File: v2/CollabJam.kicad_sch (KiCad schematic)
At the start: 35 parts, among them IC1 SIP32510DT-T1-GE3, IC2 DA7281-00V4C, IC3 DA7281-00V4C, IC4 DA7281-00V4C, IC5 DA7281-00V4C, J1 Power, J10 ESP32 right, J11 ESP32 left, J2 ESP_BAT_GND, J3 ESP_BAT_PWR, M1 M1, M2 M2, M3 M3, M4 M4

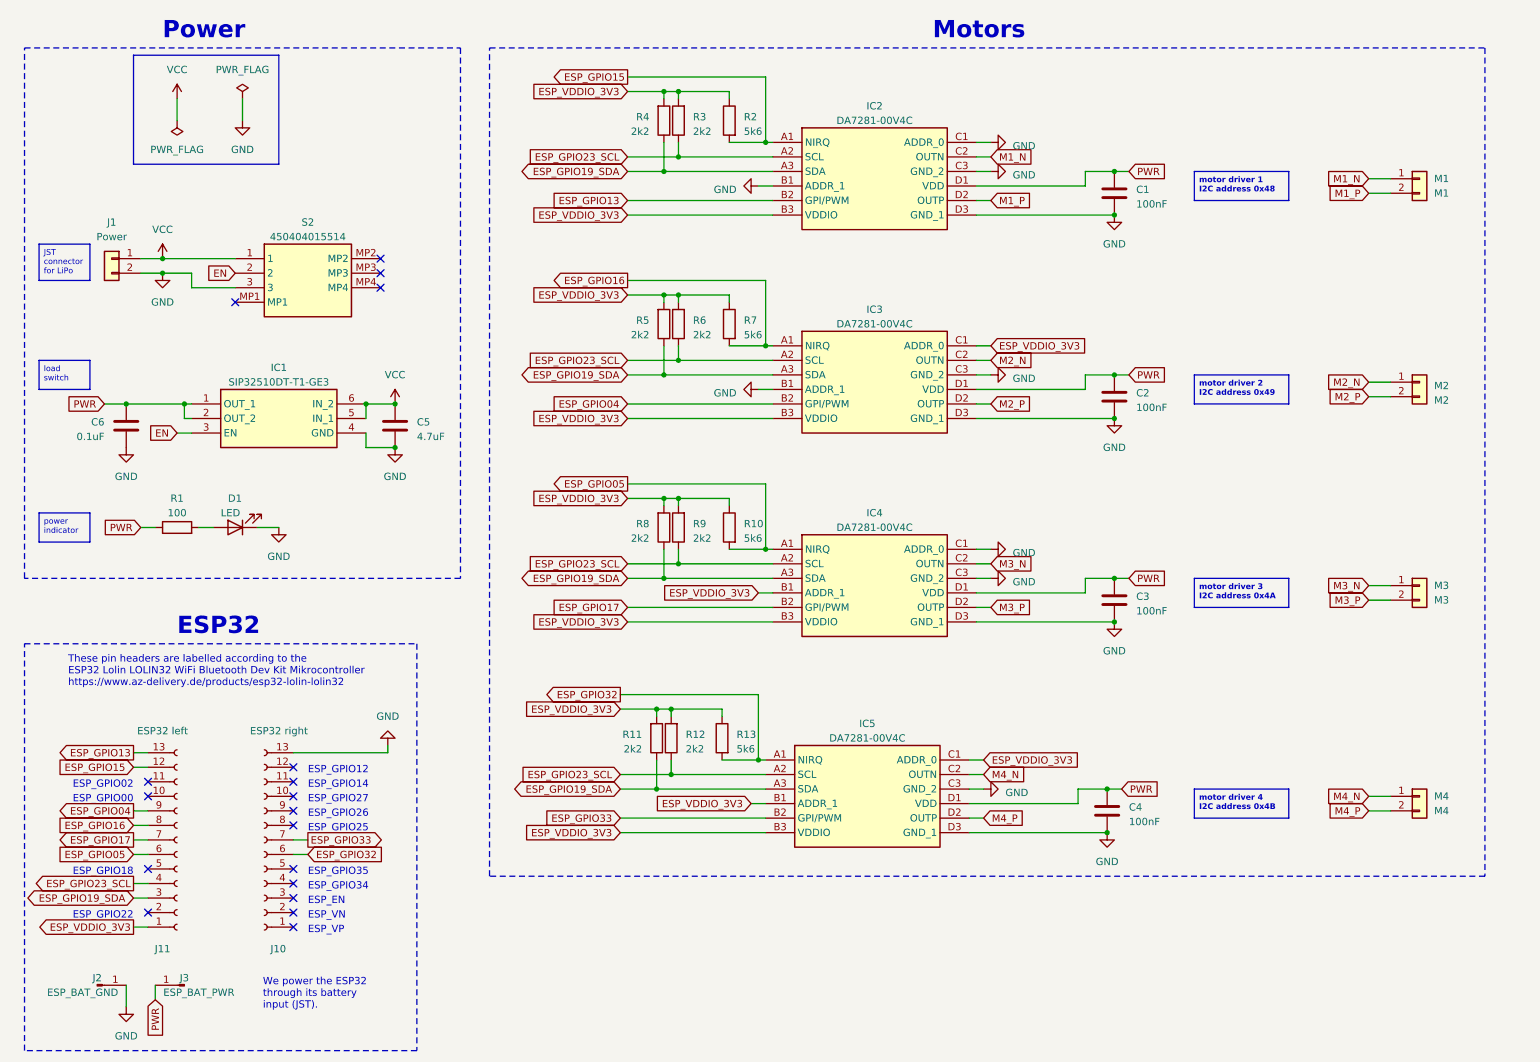
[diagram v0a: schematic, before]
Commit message: switch to QFN package for DA7281
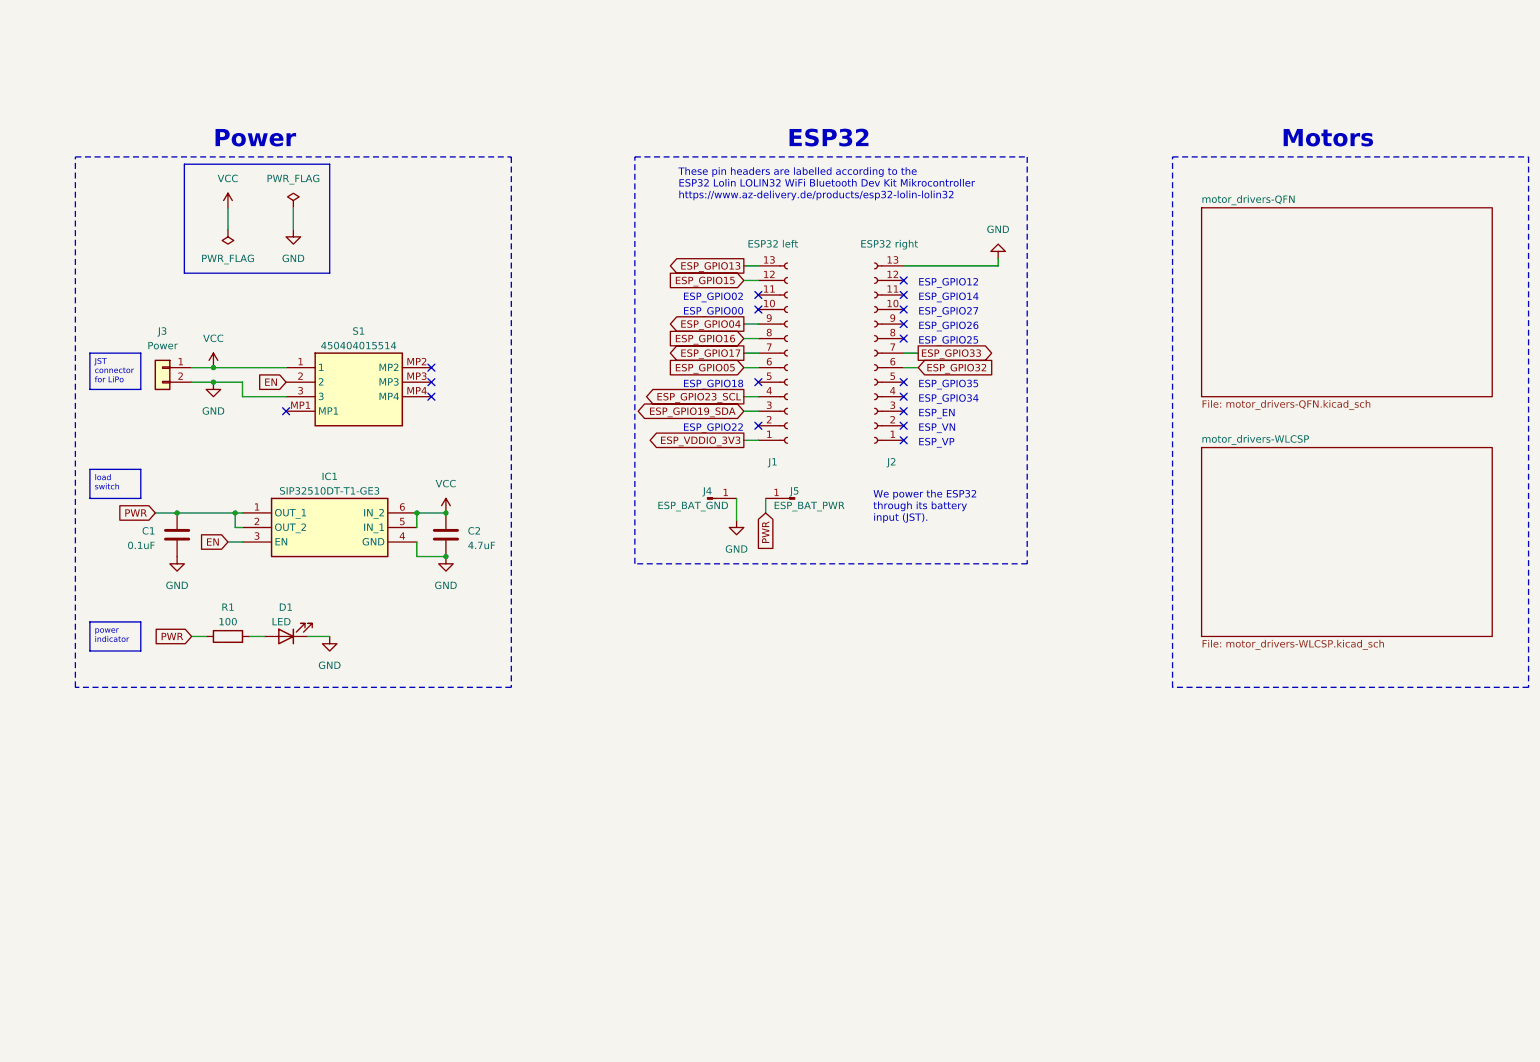
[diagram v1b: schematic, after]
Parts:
- removed C1, C2, C3, C4: 100nF, Capacitor_SMD:C_0201_0603Metric, symbol Device:C
- removed IC2, IC3, IC4, IC5: DA7281-00V4C, collabjam:BGA12C40P3X4_135X175X58, symbol CollabJam:DA7281-00V4C
- removed M1: M1, Connector_JST:JST_PH_S2B-PH-K_1x02_P2.00mm_Horizontal, symbol Connector_Generic:Conn_01x02
- removed M2: M2, Connector_JST:JST_PH_S2B-PH-K_1x02_P2.00mm_Horizontal, symbol Connector_Generic:Conn_01x02
- removed M3: M3, Connector_JST:JST_PH_S2B-PH-K_1x02_P2.00mm_Horizontal, symbol Connector_Generic:Conn_01x02
- removed M4: M4, Connector_JST:JST_PH_S2B-PH-K_1x02_P2.00mm_Horizontal, symbol Connector_Generic:Conn_01x02
- removed R10, R13, R2, R7: 5k6, Resistor_SMD:R_0201_0603Metric, symbol Device:R
- removed R11, R12, R3, R4, R5, R6, R8, R9: 2k2, Resistor_SMD:R_0201_0603Metric, symbol Device:R
- C1: renamed from C6; footprint Capacitor_SMD:C_0603_1608Metric -> Capacitor_SMD:C_0603_1608Metric_Pad1.08x0.95mm_HandSolder
- C2: renamed from C5; footprint Capacitor_SMD:C_0603_1608Metric -> Capacitor_SMD:C_0603_1608Metric_Pad1.08x0.95mm_HandSolder
- R1: footprint Resistor_SMD:R_0805_2012Metric_Pad1.20x1.40mm_HandSolder -> Resistor_SMD:R_0603_1608Metric_Pad0.98x0.95mm_HandSolder
- renumbered J11 to J1, J10 to J2, J1 to J3, J2 to J4, J3 to J5, S2 to S1
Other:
- added sheet motor_drivers-QFN (motor_drivers-QFN.kicad_sch)
- added sheet motor_drivers-WLCSP (motor_drivers-WLCSP.kicad_sch)
- moved on the sheet: C1, C2, D1, IC1, J1, J2, J3, J4, J5, R1, S1

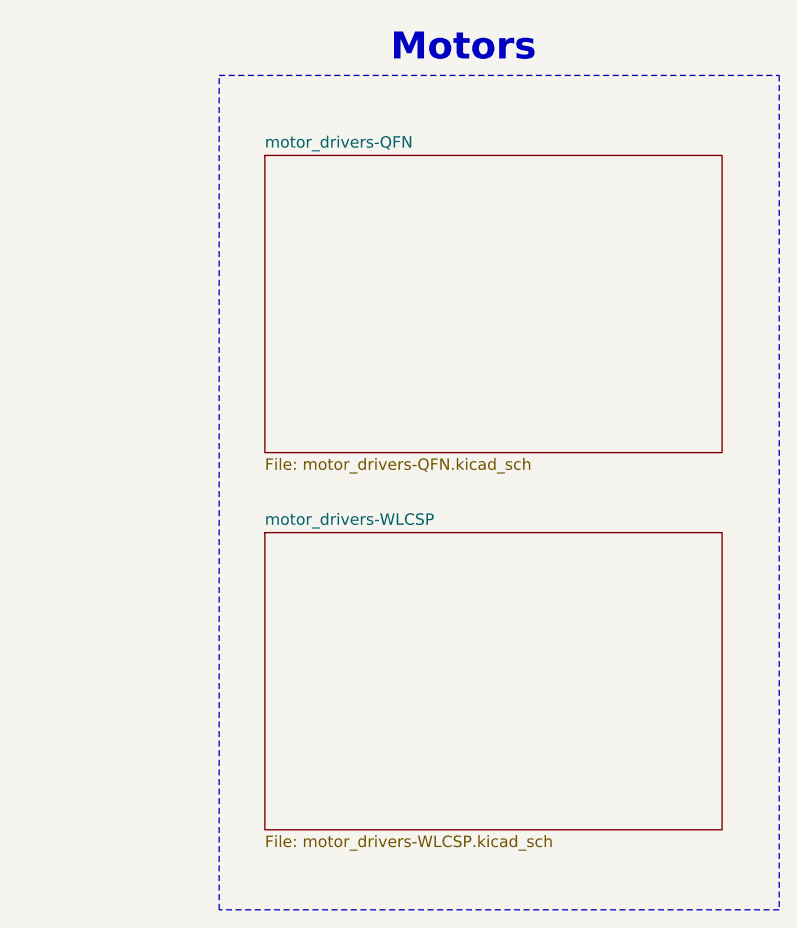
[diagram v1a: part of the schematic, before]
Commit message: start PCB layout
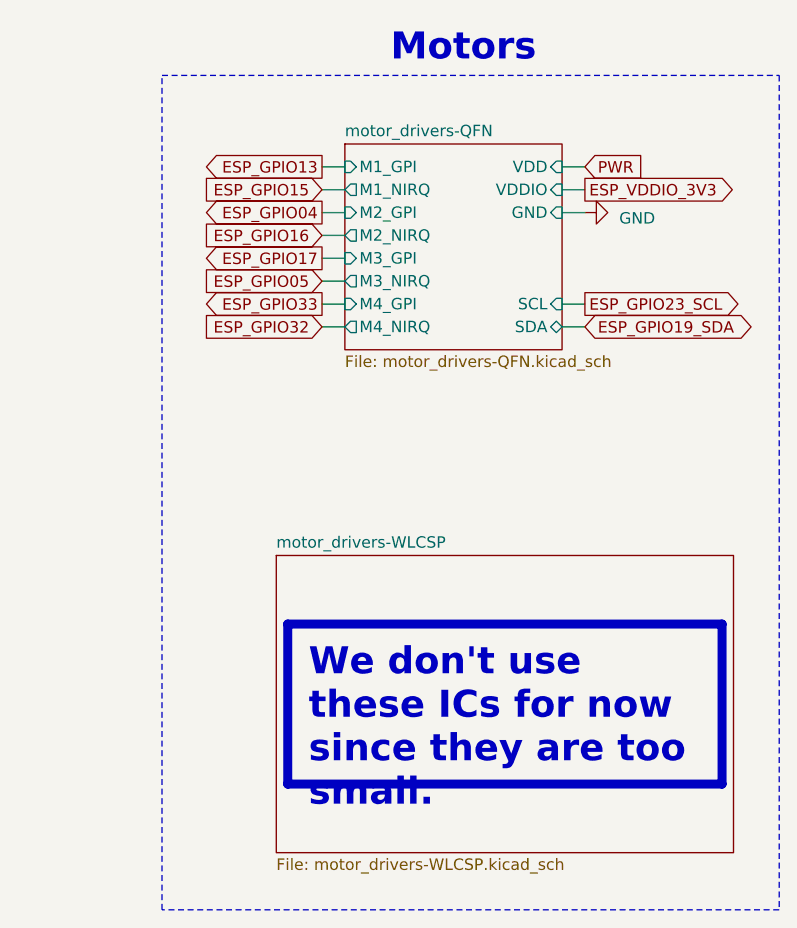
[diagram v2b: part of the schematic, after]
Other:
- sheet motor_drivers-QFN ports: added GND, M1_GPI, M1_NIRQ, M2_GPI, M2_NIRQ, M3_GPI, M3_NIRQ, M4_GPI, M4_NIRQ, SCL, SDA, VDD, VDDIO; removed none
